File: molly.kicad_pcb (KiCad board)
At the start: 2 copper layers, 71.1 x 96.5 mm, 52 parts, among them J1 QWIIC, J2 QWIIC, J3 QWIIC+, J4 QWIIC+, J5 OLED, SW1 Cherry MX, SW10 Cherry MX, SW11 Cherry MX, SW12 Cherry MX, SW13 Cherry MX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

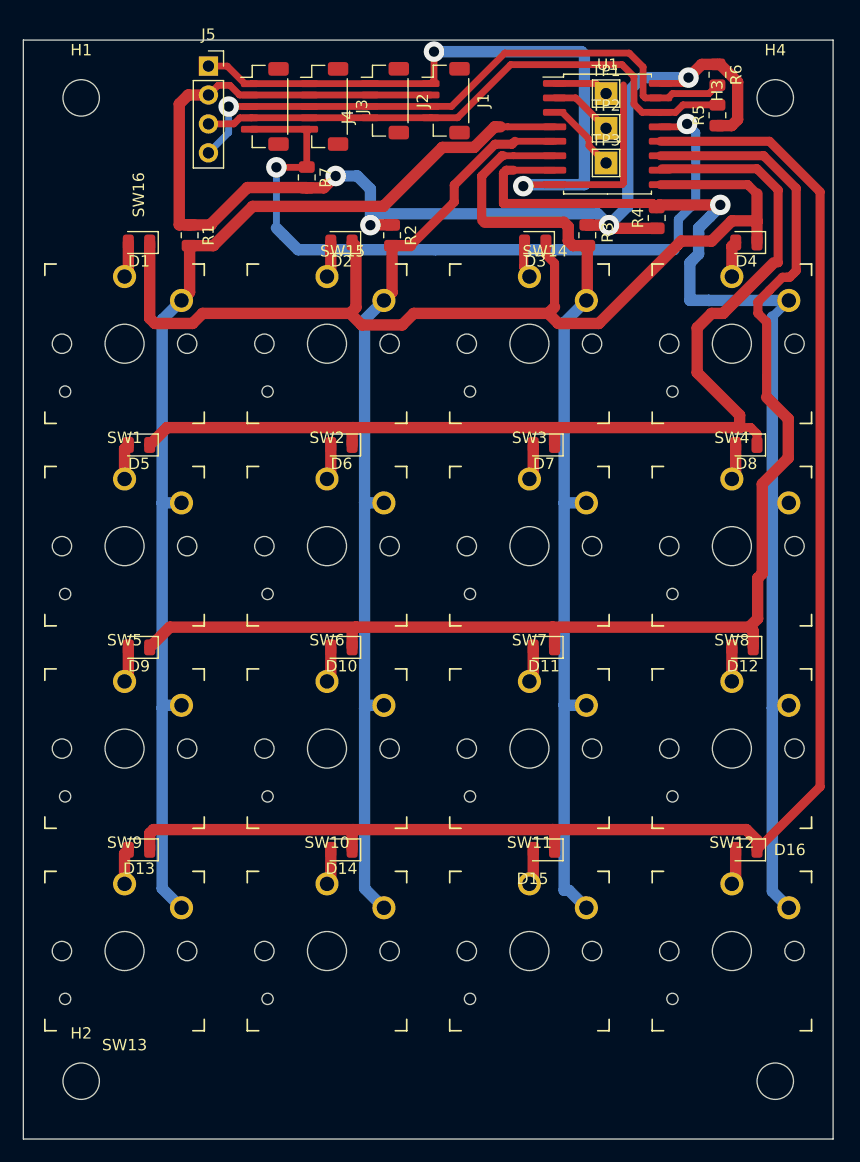
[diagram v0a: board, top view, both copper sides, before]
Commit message: Updated for more recent kicads, fix bassackwards screen pinout
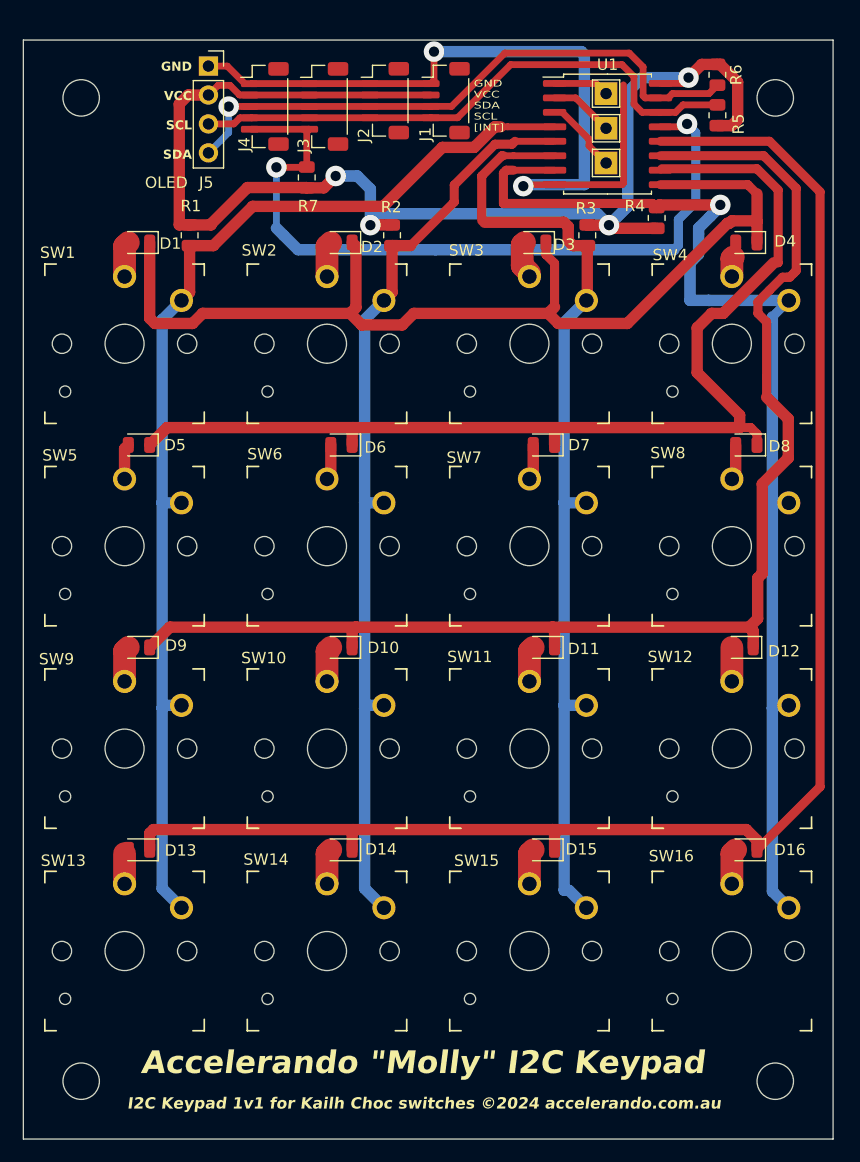
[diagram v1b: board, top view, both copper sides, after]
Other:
- board text added: "Accelerando {dblquote}Molly{dblquote} I2C Keypad"
- board text added: "GND VCC SCL SDA"
- board text added: "GND VCC SDA SCL [INT]"
- board text added: "I2C Keypad 1v1 for Kailh Choc switches ©2024 accelerando.com.au"
- board text added: "holes x 61mm holes y 86mm board x 71 board y 96.5mm"
